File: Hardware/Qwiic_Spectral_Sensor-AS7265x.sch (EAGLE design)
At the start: 51 parts, among them J2 Serial Interface, J5 Flash Programming, J8 PTH, U1 AS72651, U3 4MB Flash, U5 AS72653, U6 AS72652

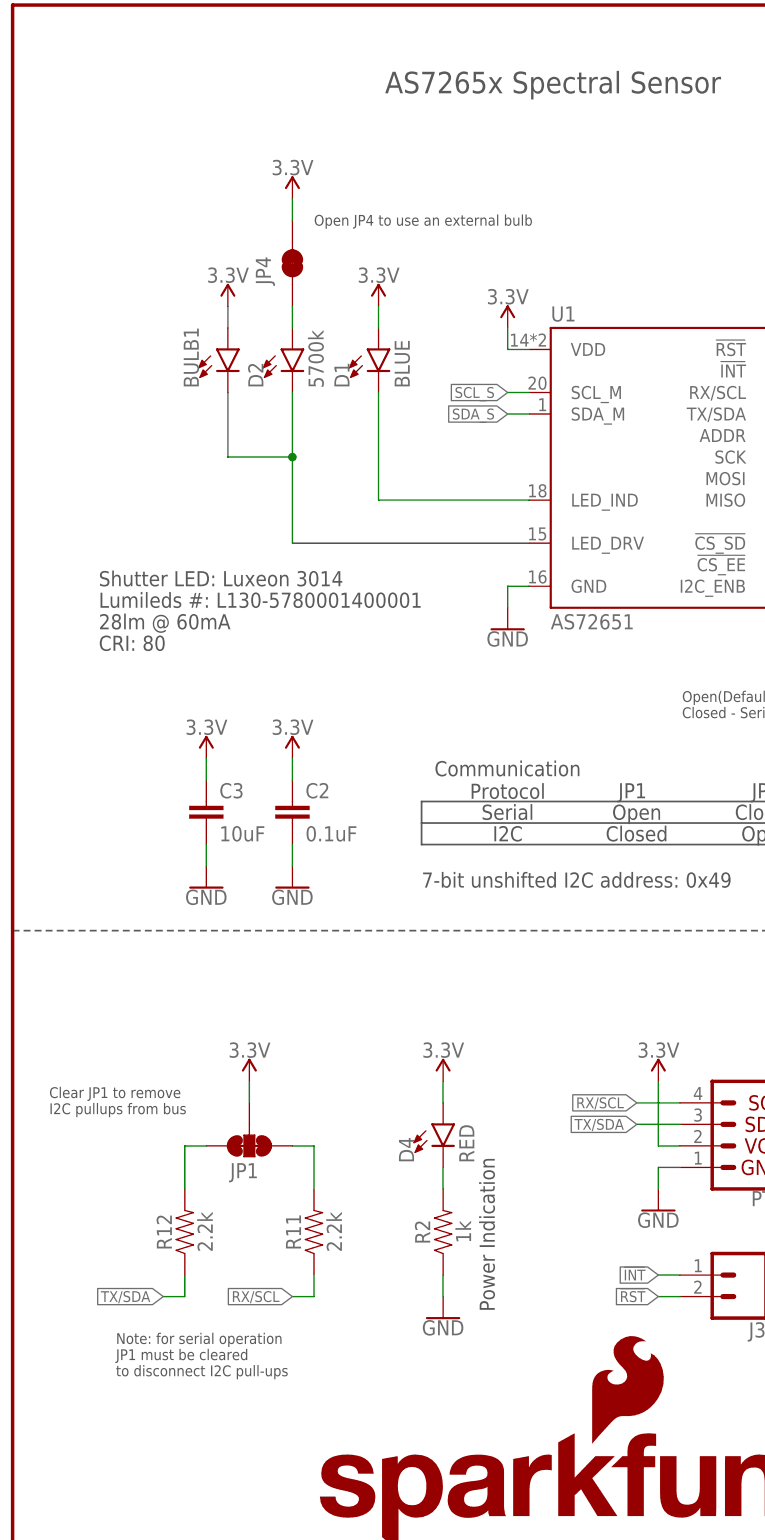
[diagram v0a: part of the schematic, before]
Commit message: Adding LED disconnect jumpers
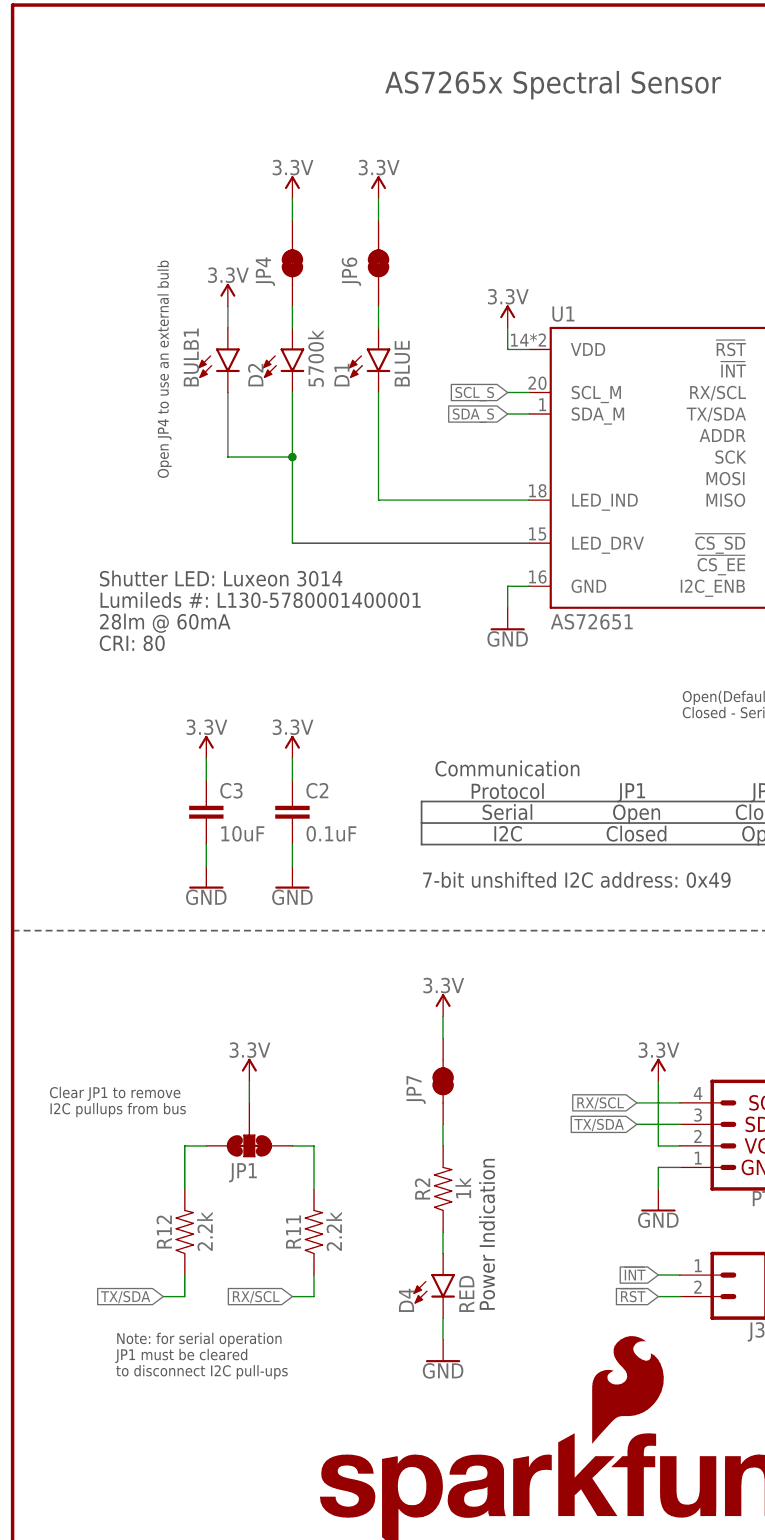
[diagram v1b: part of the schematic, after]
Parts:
- added JP6, JP7: JUMPER-SMT_2_NC_TRACE_NO-SILK, SparkFun-Jumpers:JUMPER-SMT_2_NC_TRACE_NO-SILK
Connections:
- new net N$10: D1.A, JP6.1
- new net N$7: D4.A, R2.1
- net 3.3V: now also JP6.2, JP7.2; no longer D1.A, D4.A
- net GND: now also D4.C; no longer R2.1
- net N$1: now also JP7.1; no longer D4.C
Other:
- moved on the sheet: D4, R2
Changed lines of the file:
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@@
 <part name="D3" library="SparkFun-LED" deviceset="LED-IR" device="0603" value="IR"/>
 <part name="TP1" library="SparkFun-Connectors" deviceset="TEST-POINT" device="3" value=""/>
+<part name="JP6" library="SparkFun-Jumpers" deviceset="JUMPER-SMT_2_NC_TRACE" device="_NO-SILK" value=""/>
+<part name="JP7" library="SparkFun-Jumpers" deviceset="JUMPER-SMT_2_NC_TRACE" device="_NO-SILK" value=""/>
 </parts>
 <sheets>
@@
 to disconnect I2C pull-ups </text>
 <text x="149.352" y="97.282" size="1.778" layer="97">The AS7261 must be held in reset while programming flash</text>
-<text x="35.56" y="160.02" size="1.27" layer="97" align="center-left">Open JP4 to use an external bulb</text>
+<text x="17.78" y="129.54" size="1.27" layer="97" rot="R90" align="center-left">Open JP4 to use an external bulb</text>
 <text x="58.42" y="90.17" size="1.778" layer="97" align="center">Serial</text>
 <text x="73.152" y="92.71" size="1.778" layer="97" align="center">JP1</text>
@@
 <attribute name="VALUE" x="45.085" y="140.208" size="1.778" layer="96" font="vector" rot="R90" align="top-left"/>
 </instance>
-<instance part="SUPPLY8" gate="G$1" x="43.18" y="149.86" smashed="yes">
-<attribute name="VALUE" x="43.18" y="152.654" size="1.778" layer="96" align="bottom-center"/>
+<instance part="SUPPLY8" gate="G$1" x="43.18" y="162.56" smashed="yes">
+<attribute name="VALUE" x="43.18" y="165.354" size="1.778" layer="96" align="bottom-center"/>
 </instance>
 <instance part="C3" gate="G$1" x="22.86" y="88.9" smashed="yes">
@@
 <attribute name="VALUE" x="21.844" y="40.64" size="1.778" layer="96" font="vector" rot="R90" align="top-center"/>
 </instance>
-<instance part="D4" gate="G$1" x="50.8" y="53.34" smashed="yes">
-<attribute name="NAME" x="47.371" y="48.768" size="1.778" layer="95" font="vector" rot="R90"/>
-<attribute name="VALUE" x="52.705" y="48.768" size="1.778" layer="96" font="vector" rot="R90" align="top-left"/>
-</instance>
-<instance part="SUPPLY22" gate="G$1" x="50.8" y="58.42" smashed="yes" rot="MR0">
-<attribute name="VALUE" x="50.8" y="61.214" size="1.778" layer="96" rot="MR0" align="bottom-center"/>
-</instance>
-<instance part="R2" gate="G$1" x="50.8" y="40.64" smashed="yes" rot="R90">
-<attribute name="NAME" x="49.276" y="40.64" size="1.778" layer="95" font="vector" rot="R90" align="bottom-center"/>
-<attribute name="VALUE" x="52.324" y="40.64" size="1.778" layer="96" font="vector" rot="R90" align="top-center"/>
-</instance>
-<instance part="GND22" gate="1" x="50.8" y="30.48" smashed="yes" rot="MR0">
-<attribute name="VALUE" x="50.8" y="30.226" size="1.778" layer="96" rot="MR0" align="top-center"/>
+<instance part="D4" gate="G$1" x="50.8" y="35.56" smashed="yes">
+<attribute name="NAME" x="47.371" y="30.988" size="1.778" layer="95" font="vector" rot="R90"/>
+<attribute name="VALUE" x="52.705" y="30.988" size="1.778" layer="96" font="vector" rot="R90" align="top-left"/>
+</instance>
+<instance part="SUPPLY22" gate="G$1" x="50.8" y="66.04" smashed="yes" rot="MR0">
+<attribute name="VALUE" x="50.8" y="68.834" size="1.778" layer="96" rot="MR0" align="bottom-center"/>
+</instance>
+<instance part="R2" gate="G$1" x="50.8" y="45.72" smashed="yes" rot="R90">
+<attribute name="NAME" x="49.276" y="45.72" size="1.778" layer="95" font="vector" rot="R90" align="bottom-center"/>
+<attribute name="VALUE" x="52.324" y="45.72" size="1.778" layer="96" font="vector" rot="R90" align="top-center"/>
+</instance>
+<instance part="GND22" gate="1" x="50.8" y="25.4" smashed="yes" rot="MR0">
+<attribute name="VALUE" x="50.8" y="25.146" size="1.778" layer="96" rot="MR0" align="top-center"/>
 </instance>
 <instance part="FD3" gate="G$1" x="236.22" y="27.94" smashed="yes"/>
@@
 <attribute name="VALUE" x="111.76" y="114.3" size="1.778" layer="96" font="vector"/>
 </instance>
+<instance part="JP6" gate="G$1" x="43.18" y="154.94" smashed="yes" rot="R90">
+<attribute name="NAME" x="40.64" y="152.4" size="1.778" layer="95" font="vector" rot="R90"/>
+<attribute name="VALUE" x="45.72" y="152.4" size="1.778" layer="96" font="vector" rot="R90" align="top-left"/>
+</instance>
+<instance part="JP7" gate="G$1" x="50.8" y="58.42" smashed="yes" rot="R90">
+<attribute name="NAME" x="48.26" y="55.88" size="1.778" layer="95" font="vector" rot="R90"/>
+<attribute name="VALUE" x="53.34" y="55.88" size="1.778" layer="96" font="vector" rot="R90" align="top-left"/>
+</instance>
 </instances>
 <busses>
@@
 </segment>
 <segment>
-<pinref part="R2" gate="G$1" pin="1"/>
 <pinref part="GND22" gate="1" pin="GND"/>
-<wire x1="50.8" y1="33.02" x2="50.8" y2="35.56" width="0.1524" layer="91"/>
+<pinref part="D4" gate="G$1" pin="C"/>
+<wire x1="50.8" y1="30.48" x2="50.8" y2="27.94" width="0.1524" layer="91"/>
 </segment>
 </net>
@@
 </segment>
 <segment>
-<pinref part="D1" gate="G$1" pin="A"/>
-<pinref part="SUPPLY8" gate="G$1" pin="3.3V"/>
-<wire x1="43.18" y1="147.32" x2="43.18" y2="149.86" width="0.1524" layer="91"/>
-</segment>
-<segment>
 <pinref part="C3" gate="G$1" pin="1"/>
 <pinref part="SUPPLY10" gate="G$1" pin="3.3V"/>
@@
 </segment>
 <segment>
-<pinref part="D4" gate="G$1" pin="A"/>
 <pinref part="SUPPLY22" gate="G$1" pin="3.3V"/>
-<wire x1="50.8" y1="58.42" x2="50.8" y2="55.88" width="0.1524" layer="91"/>
+<wire x1="50.8" y1="63.5" x2="50.8" y2="66.04" width="0.1524" layer="91"/>
+<pinref part="JP7" gate="G$1" pin="2"/>
+</segment>
+<segment>
+<pinref part="SUPPLY8" gate="G$1" pin="3.3V"/>
+<pinref part="JP6" gate="G$1" pin="2"/>
+<wire x1="43.18" y1="160.02" x2="43.18" y2="162.56" width="0.1524" layer="91"/>
 </segment>
 </net>
@@
 <net name="N$1" class="0">
 <segment>
-<pinref part="D4" gate="G$1" pin="C"/>
 <pinref part="R2" gate="G$1" pin="2"/>
-<wire x1="50.8" y1="45.72" x2="50.8" y2="48.26" width="0.1524" layer="91"/>
-</segment>
-</net>
+<wire x1="50.8" y1="50.8" x2="50.8" y2="53.34" width="0.1524" layer="91"/>
+<pinref part="JP7" gate="G$1" pin="1"/>
+</segment>
+</net>
+<net name="N$7" class="0">
+<segment>
+<pinref part="D4" gate="G$1" pin="A"/>
+<pinref part="R2" gate="G$1" pin="1"/>
+<wire x1="50.8" y1="40.64" x2="50.8" y2="38.1" width="0.1524" layer="91"/>
+</segment>
+</net>
+<net name="N$10" class="0">
+<segment>
+<pinref part="D1" gate="G$1" pin="A"/>
+<pinref part="JP6" gate="G$1" pin="1"/>
+<wire x1="43.18" y1="149.86" x2="43.18" y2="147.32" width="0.1524" layer="91"/>
+</segment>
+</net>

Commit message: Commit before panels
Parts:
- removed JP6: JUMPER-SMT_2_NC_TRACE_NO-SILK, SparkFun-Jumpers:JUMPER-SMT_2_NC_TRACE_NO-SILK
- removed U6: AS72652, Qwiic_Spectral_Sensor-AS7265x:AS72652
- added U2: 4MB Flash, SparkFun-IC-Memory:AT25SF041
- U3: value 4MB Flash -> AS72652; device SparkFun-IC-Memory:AT25SF041 -> Qwiic_Spectral_Sensor-AS7265x:AS72652
- renumbered U5 to U4
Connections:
- removed net N$10: D1.A, JP6.1
- net !CS_EE: now also U2.!CS; no longer U3.!CS
- net !RST-ADDR: now also U3.!RST; no longer U6.!RST
- net 3.3V: now also D1.A, U2.!HOLD(D3), U2.!WP(D2), U2.VCC, U3.VDD; no longer JP6.2, U3.!HOLD(D3), U3.!WP(D2), U3.VCC, U6.VDD
- net GND: now also U2.GND; no longer U6.GND
- net LED_DRV1: now also U3.LED_DRV; no longer U6.LED_DRV
- net MISO: now also U2.SO(D1); no longer U3.SO(D1)
- net MOSI: now also U2.SI(D0); no longer U3.SI(D0)
- net N$3: now also U3.!CS_SD; no longer U6.!CS_SD
- net N$9: now also U3.MISO; no longer U6.MISO
- net SCK: now also U2.SCK; no longer U3.SCK
- net SCL_S: now also U3.SCL_S; no longer U6.SCL_S
- net SDA_S: now also U3.SDA_S; no longer U6.SDA_S
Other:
- moved on the sheet: BULB1, BULB2, BULB3, D1, D2, D3, D5, JP3, JP4, JP5, R10, R9
